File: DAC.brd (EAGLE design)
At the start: 81.3 x 82.5 mm, 97 parts, among them IC1 LM2662, IC2 PCM1793, IC3 OPA2134PA, IC4 LMH6643, J1 USBSMD, J2 RCJ-21XXMILL, U1 LDO-TPS78233, U2 PCM2707, Y1 12MHz/20pF

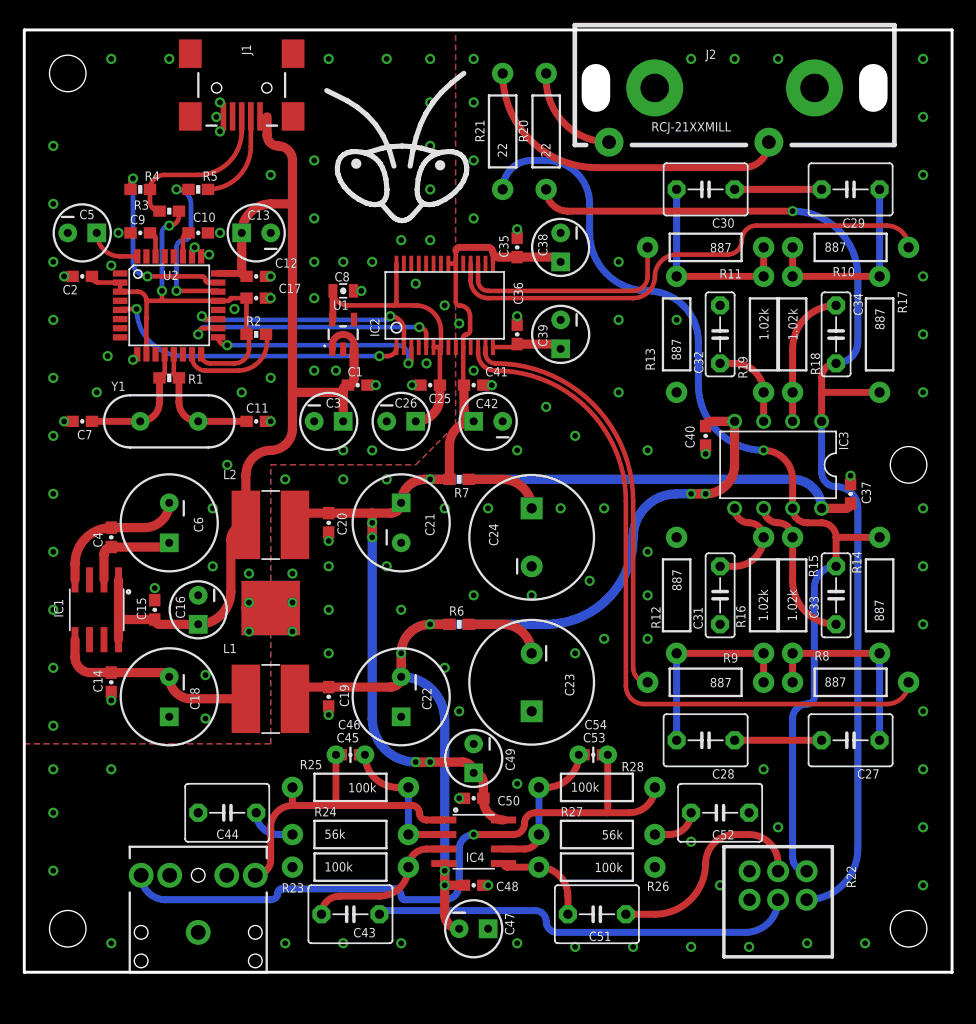
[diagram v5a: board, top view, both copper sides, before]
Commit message: Mounting holes
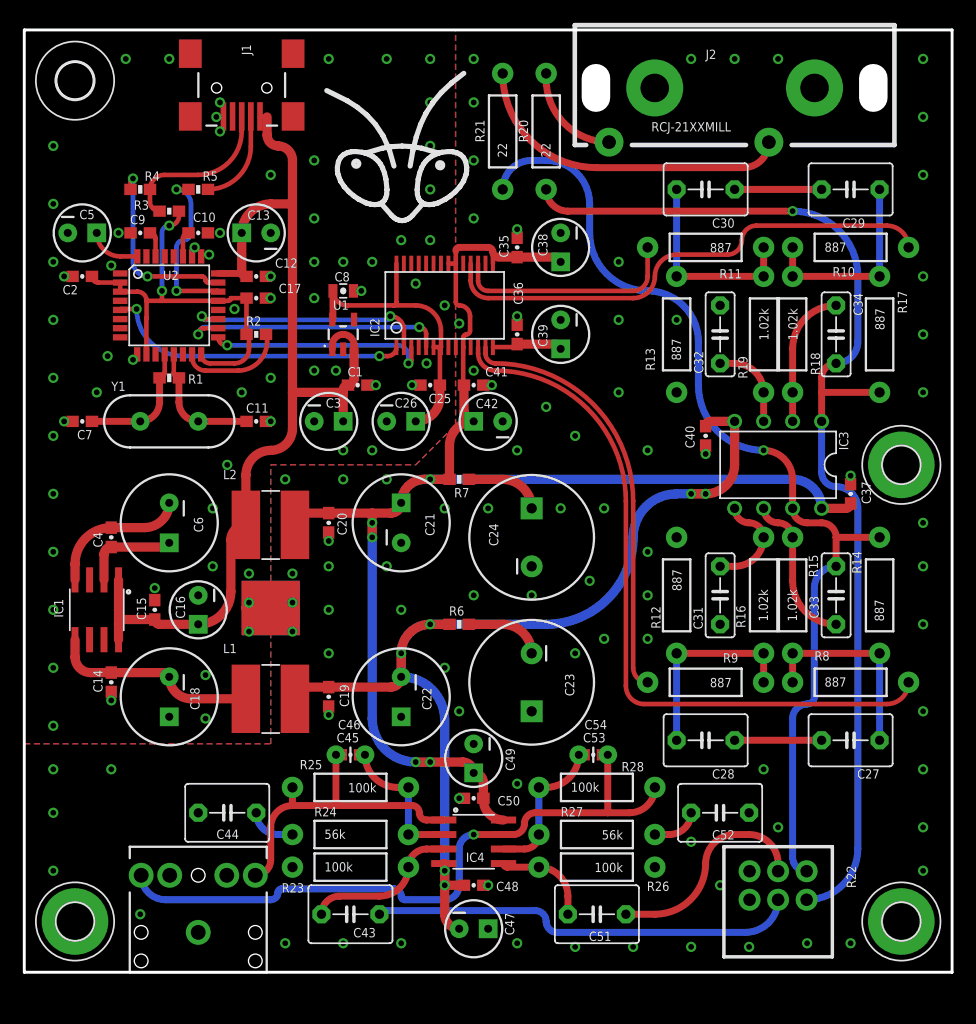
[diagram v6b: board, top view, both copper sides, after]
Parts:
- added H1, H2, H3: MOUNT-PAD-ROUND3.2, holes:3,2-PAD
- added H4: MOUNT-HOLE3.2, holes:3,2
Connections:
- net AGND: now also H1.B3,2, H2.B3,2, H3.B3,2
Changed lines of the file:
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@@
 <wire x1="81.28" y1="0" x2="0" y2="0" width="0.254" layer="20"/>
 <wire x1="0" y1="0" x2="0" y2="82.55" width="0.254" layer="20"/>
-<hole x="77.47" y="44.45" drill="3.2"/>
-<hole x="77.47" y="3.81" drill="3.2"/>
-<hole x="3.81" y="3.81" drill="3.2"/>
-<hole x="3.81" y="78.74" drill="3.2"/>
 <dimension x1="0" y1="82.55" x2="81.28" y2="82.55" x3="40.64" y3="88.9" textsize="1.778" layer="47"/>
 <dimension x1="0" y1="82.55" x2="0" y2="0" x3="-6.35" y3="41.275" textsize="1.778" layer="47" dtype="vertical"/>
@@
 <attribute name="VALUE" x="63.5" y="16.256" size="0.8128" layer="27" ratio="20" rot="R180"/>
 </element>
+<element name="H1" library="holes" package="3,2-PAD" value="MOUNT-PAD-ROUND3.2" x="76.835" y="4.445"/>
+<element name="H2" library="holes" package="3,2-PAD" value="MOUNT-PAD-ROUND3.2" x="4.445" y="4.445"/>
+<element name="H3" library="holes" package="3,2-PAD" value="MOUNT-PAD-ROUND3.2" x="76.835" y="44.45"/>
+<element name="H4" library="holes" package="3,2" value="MOUNT-HOLE3.2" x="4.445" y="78.105"/>
 </elements>
 <signals>
@@
 <via x="2.54" y="67.31" extent="1-16" drill="0.5"/>
 <via x="2.54" y="72.39" extent="1-16" drill="0.5"/>
-<via x="7.62" y="80.01" extent="1-16" drill="0.5"/>
+<via x="8.89" y="80.01" extent="1-16" drill="0.5"/>
 <via x="12.7" y="80.01" extent="1-16" drill="0.5"/>
 <via x="26.67" y="80.01" extent="1-16" drill="0.5"/>
@@
 <via x="78.74" y="55.88" extent="1-16" drill="0.5"/>
 <via x="78.74" y="50.8" extent="1-16" drill="0.5"/>
-<via x="78.74" y="40.64" extent="1-16" drill="0.5"/>
+<via x="78.74" y="39.37" extent="1-16" drill="0.5"/>
 <via x="78.74" y="35.56" extent="1-16" drill="0.5"/>
 <via x="78.74" y="30.48" extent="1-16" drill="0.5"/>
 <via x="78.74" y="22.86" extent="1-16" drill="0.5"/>
 <via x="78.74" y="17.78" extent="1-16" drill="0.5"/>
-<via x="78.74" y="7.62" extent="1-16" drill="0.5"/>
+<via x="78.74" y="8.89" extent="1-16" drill="0.5"/>
 <via x="40.64" y="7.62" extent="1-16" drill="0.5"/>
 <via x="43.18" y="16.51" extent="1-16" drill="0.5"/>
@@
 <via x="38.1" y="15.24" extent="1-16" drill="0.5"/>
 <via x="2.54" y="8.89" extent="1-16" drill="0.5"/>
-<via x="7.62" y="2.54" extent="1-16" drill="0.5"/>
+<via x="10.16" y="5.08" extent="1-16" drill="0.5"/>
 <via x="22.86" y="2.54" extent="1-16" drill="0.5"/>
 <via x="27.94" y="2.54" extent="1-16" drill="0.5"/>
@@
 <via x="63.5" y="2.2225" extent="1-16" drill="0.5"/>
 <via x="68.58" y="2.54" extent="1-16" drill="0.5"/>
-<via x="73.66" y="2.54" extent="1-16" drill="0.5"/>
+<via x="72.39" y="2.54" extent="1-16" drill="0.5"/>
 <via x="78.74" y="12.7" extent="1-16" drill="0.5"/>
 <via x="58.42" y="11.43" extent="1-16" drill="0.5"/>
@@
 <contactref element="C52" pad="1"/>
 <contactref element="C44" pad="1"/>
+<contactref element="H3" pad="B3,2"/>
+<contactref element="H1" pad="B3,2"/>
+<contactref element="H2" pad="B3,2"/>
 </signal>
 <signal name="3V3">
